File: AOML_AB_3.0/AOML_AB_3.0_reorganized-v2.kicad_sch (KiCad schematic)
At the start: 98 parts, among them IC11 SN74LVC1G3157DCKR, J1 Conn_01x04, J2 216550-1, J4 Conn_01x07, J5 Screw_Terminal_01x04, J6 Conn_01x03, J7 Screw_Terminal_01x07, SW1 TS02-66-70-BK-160-LCR-D, U1 L7812ABD2T-TR, U2 LM7805MPX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

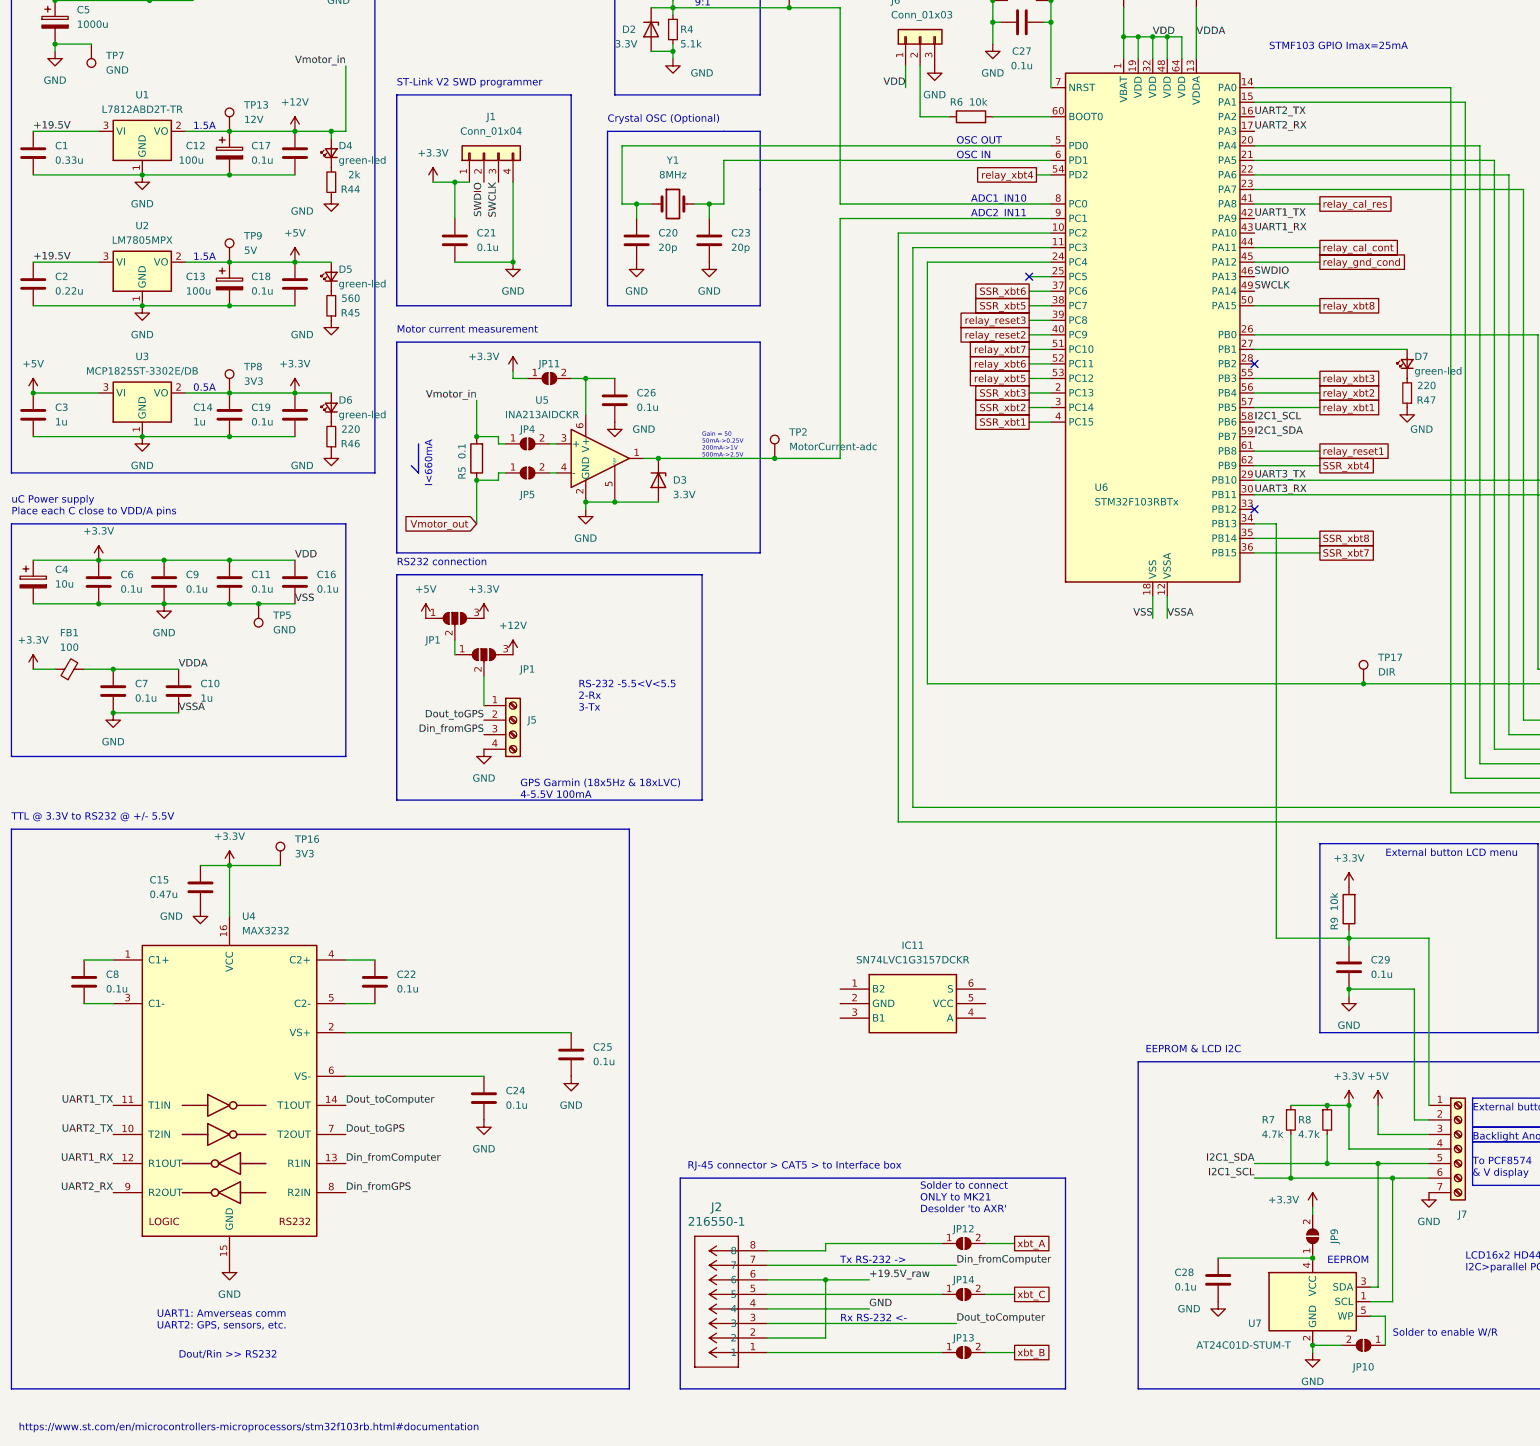
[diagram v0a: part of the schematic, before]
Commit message: PCB v2 final: added multiplexer for Tx (from STM32 uart1 OR GPS), GPS only 3 pins (pwr, gnd, Tx), Auxiliary test connectors RS232+PWR added, thin track thickness changed (0.15 to 0.155 mm)
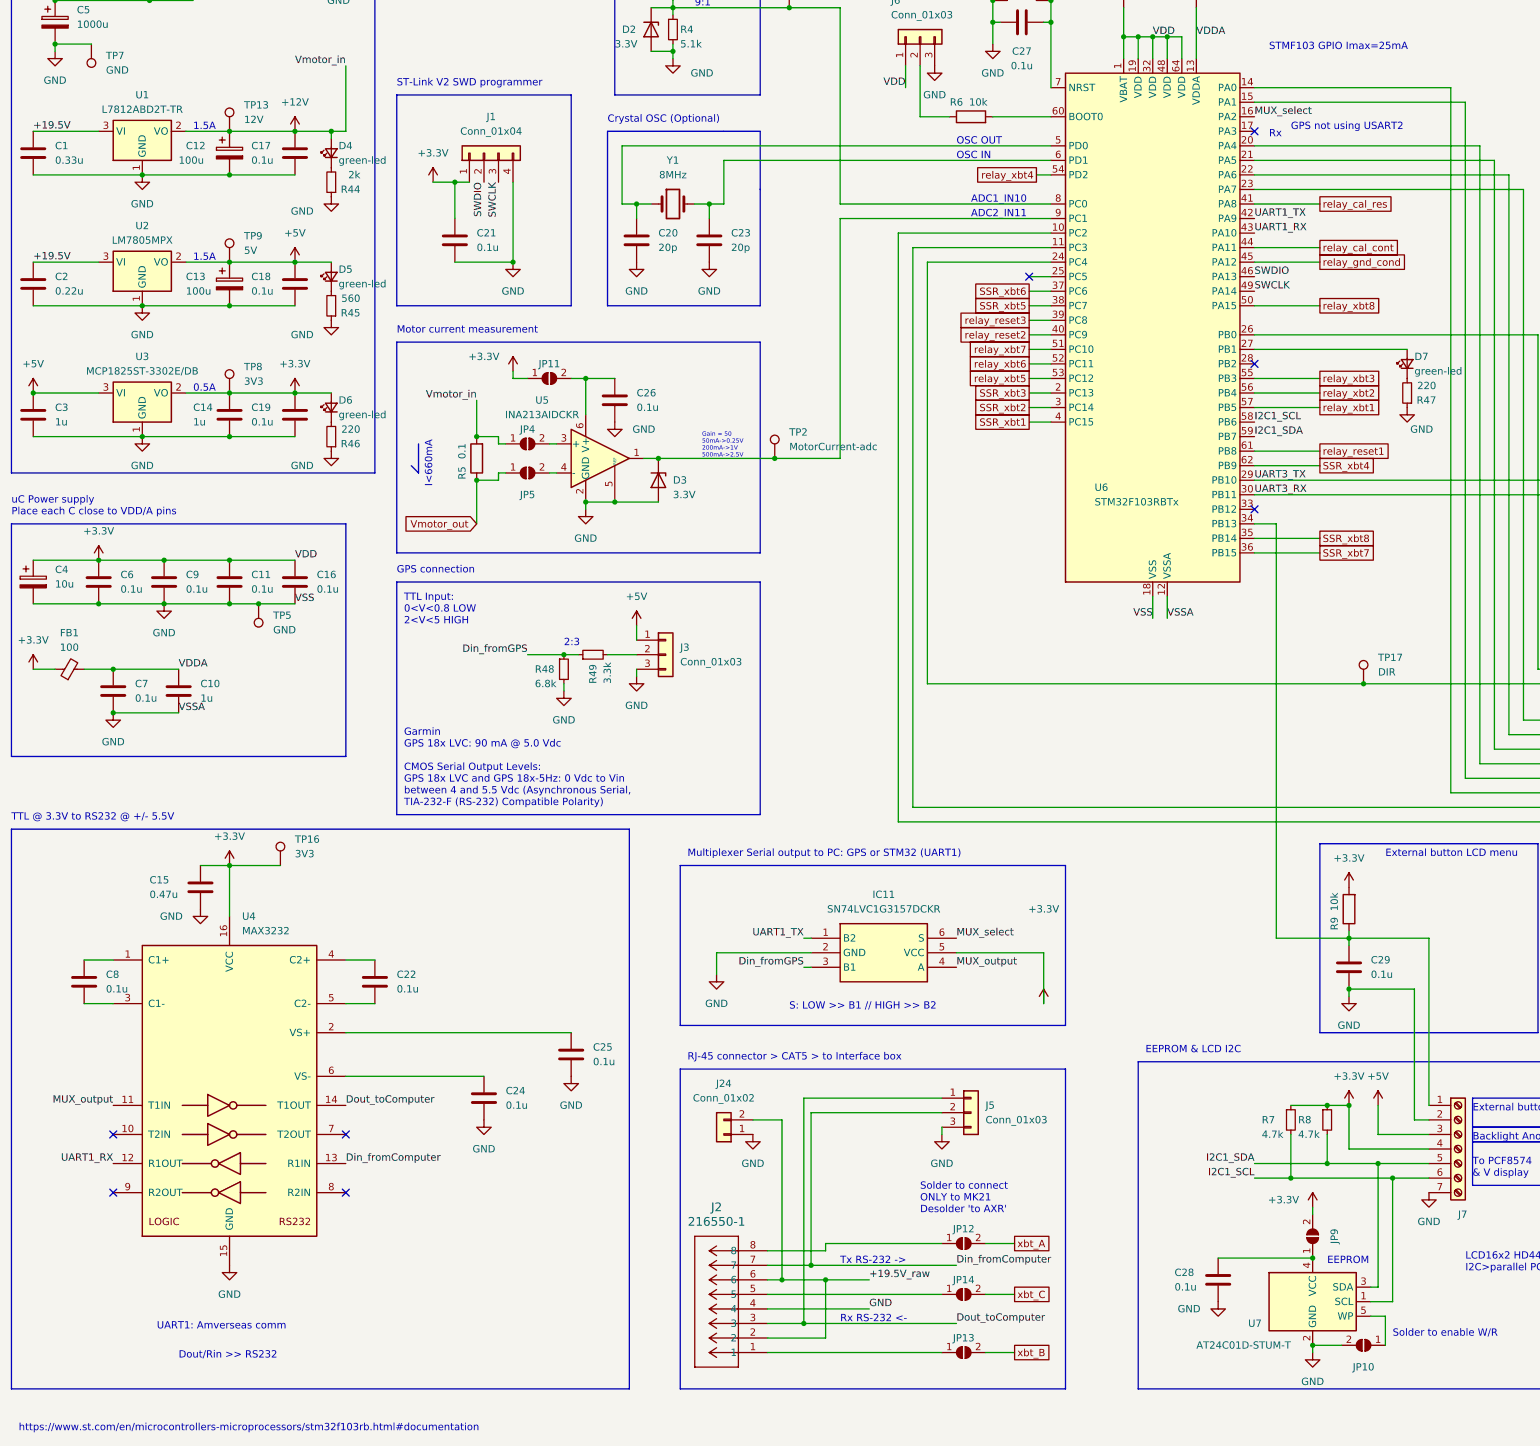
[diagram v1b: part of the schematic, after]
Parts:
- removed J5: Screw_Terminal_01x04, Header_screw_4x1_TB001-500-04BE:CUI_TB001-500-04BE, symbol Connector:Screw_Terminal_01x04
- removed JP1 (x2): SolderJumper_3_Open, Jumper:SolderJumper-3_P1.3mm_Open_RoundedPad1.0x1.5mm, symbol Jumper:SolderJumper_3_Open
- added J24: Conn_01x02, Connector_PinSocket_2.54mm:PinSocket_1x02_P2.54mm_Vertical, symbol Connector_Generic:Conn_01x02
- added J3: Conn_01x03, CUI_3x1_connector:CUI_TBP02R2-381-03BE, symbol Connector_Generic:Conn_01x03
- added J5: Conn_01x03, Connector_PinSocket_2.54mm:PinSocket_1x03_P2.54mm_Vertical, symbol Connector_Generic:Conn_01x03
- added R48: 6.8k, Resistor_0805:RC0805N_YAG, symbol Device:R_Small
- added R49: 3.3k, Resistor_0805:RC0805N_YAG, symbol Device:R_Small
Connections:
- net +19.5V_raw: now also J24.2 (Pin_2)
- net +3.3V: now also IC11.5 (VCC)
- net +5V: now also J3.1 (Pin_1)
- net Din_fromComputer: now also J5.2 (Pin_2)
- net Din_fromGPS: now also IC11.3 (B1), R48.1, R49.1; no longer U4.8 (R2IN)
- net Dout_toComputer: now also J5.1 (Pin_1)
- net GND: now also IC11.2 (GND), J24.1 (Pin_1), J3.3 (Pin_3), J5.3 (Pin_3), R48.2
- net UART1_TX: now also IC11.1 (B2); no longer U4.11 (T1IN)
- net MUX_output: now reaches IC11.4 (A)
- net MUX_output: now also U4.11 (T1IN)
- net MUX_select: now reaches IC11.6 (S)
- net MUX_select: now also U6.16 (PA2)
- net Dout_toGPS: no longer names the net of U4.7 (T2OUT)
- net UART2_RX: no longer names the net of U4.9 (R2OUT)
- net UART2_RX: no longer U6.17 (PA3)
- net UART2_TX: no longer names the net of U4.10 (T2IN)
- net UART2_TX: no longer U6.16 (PA2)
- new net: J3.2 (Pin_2), R49.2
- no-connect marks 3 -> 8
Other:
- note added: "GPS connection"
- note added: "GPS not using USART2"
- note added: "Garmin GPS 18x LVC: 90 mA @ 5.0 Vdc CMOS Serial Output Levels: GPS 18x LVC and GPS 18x-5Hz: 0 Vdc to Vin between 4 and 5.5 Vdc (Asynchronous Serial, TIA-232-F (RS-232) Compatible Polarity)"
- note added: "Multiplexer Serial output to PC: GPS or STM32 (UART1)"
- note added: "Rx"
- note added: "S: LOW >> B1 // HIGH >> B2"
- note added: "TTL Input: 0<V<0.8 LOW 2<V<5 HIGH"
- note added: "UART1: Amverseas comm"
- note removed: "GPS Garmin (18x5Hz & 18xLVC) 4-5.5V 100mA"
- note removed: "RS-232 -5.5<V<5.5 2-Rx 3-Tx"
- note removed: "RS232 connection"
- note removed: "UART1: Amverseas comm UART2: GPS, sensors, etc."
- moved on the sheet: IC11

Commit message: New version v3, in assembly process and noting changes for next revision
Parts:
- added FID1, FID2, FID3: Fiducial, Fiducial:Fiducial_0.75mm_Mask1.5mm, symbol Mechanical:Fiducial
- IC11: Cost (none) -> 0.34; Digikey (none) -> https://www.digikey.com/en/products/detail/texas-instrument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; Height 1.1 -> (none); Manufacturer_Name Texas Instruments -> (none); Manufacturer_Part_Number SN74LVC1G3157DCKR -> (none); Mouser Part Number 595-SN74LVC1G3157DCK -> (none); Mouser Price/Stock https://www.mouser.co.uk/ProductDetail/Texas-Instruments/SN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 -> (none)
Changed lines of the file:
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@@
     )
   )
+  (symbol (lib_id "Mechanical:Fiducial") (at 304.8 46.99 0) (unit 1)
+    (in_bom yes) (on_board yes) (dnp no) (fields_autoplaced)
+    (property "Reference" "FID3" (at 307.34 45.72 0)
+      (effects (font (size 1.27 1.27)) (justify left))
+    )
+    (property "Value" "Fiducial" (at 307.34 48.26 0)
+      (effects (font (size 1.27 1.27)) (justify left))
+    )
+    (property "Footprint" "Fiducial:Fiducial_0.75mm_Mask1.5mm" (at 304.8 46.99 0)
+      (effects (font (size 1.27 1.27)) hide)
+    )
+    (property "Datasheet" "~" (at 304.8 46.99 0)
+      (effects (font (size 1.27 1.27)) hide)
+    )
+    (instances
+      (project "AOML_AB_3.0_reorganized-v2"
+        (path "/6a222f58-627e-41ff-951d-9ad8d2e0d7a2"
+          (reference "FID3") (unit 1)
+        )
+      )
+    )
+  )
   (symbol (lib_id "power:GND") (at 175.26 44.45 0) (unit 1)
     (in_bom yes) (on_board yes) (dnp no) (fields_autoplaced)
@@
       (effects (font (size 1.27 1.27)) hide)
     )
-    (property "Datasheet" "" (at 69.85 109.22 0)
+    (property "Datasheet" "https://www.yageo.com/upload/media/product/products/datasheet/rchip/PYu-RC_Group_51_RoHS_L_12.pdf" (at 69.85 109.22 0)
       (effects (font (size 1.27 1.27)) hide)
     )
@@
       (effects (font (size 1.27 1.27)) hide)
     )
-    (property "Datasheet" "" (at 257.81 101.6 0)
+    (property "Datasheet" "https://www.yageo.com/upload/media/product/products/datasheet/rchip/PYu-RC_Group_51_RoHS_L_12.pdf" (at 257.81 101.6 0)
       (effects (font (size 1.27 1.27)) hide)
     )
@@
     )
   )
+  (symbol (lib_id "Mechanical:Fiducial") (at 304.8 31.75 0) (unit 1)
+    (in_bom yes) (on_board yes) (dnp no) (fields_autoplaced)
+    (property "Reference" "FID1" (at 307.34 30.48 0)
+      (effects (font (size 1.27 1.27)) (justify left))
+    )
+    (property "Value" "Fiducial" (at 307.34 33.02 0)
+      (effects (font (size 1.27 1.27)) (justify left))
+    )
+    (property "Footprint" "Fiducial:Fiducial_0.75mm_Mask1.5mm" (at 304.8 31.75 0)
+      (effects (font (size 1.27 1.27)) hide)
+    )
+    (property "Datasheet" "~" (at 304.8 31.75 0)
+      (effects (font (size 1.27 1.27)) hide)
+    )
+    (instances
+      (project "AOML_AB_3.0_reorganized-v2"
+        (path "/6a222f58-627e-41ff-951d-9ad8d2e0d7a2"
+          (reference "FID1") (unit 1)
+        )
+      )
+    )
+  )
   (symbol (lib_id "Connector:TestPoint") (at 57.15 138.43 180) (unit 1)
     (in_bom yes) (on_board yes) (dnp no) (fields_autoplaced)
@@
       (effects (font (size 1.27 1.27)) (justify left top) hide)
     )
-    (property "Height" "1.1" (at 175.26 591.77 0)
-      (effects (font (size 1.27 1.27)) (justify left top) hide)
-    )
-    (property "Mouser Part Number" "595-SN74LVC1G3157DCK" (at 175.26 691.77 0)
-      (effects (font (size 1.27 1.27)) (justify left top) hide)
-    )
-    (property "Mouser Price/Stock" "https://www.mouser.co.uk/ProductDetail/Texas-Instruments/SN74LVC1G3157DCKR?qs=PVVDbbWpW3J21wbz0QWbxg%3D%3D" (at 175.26 791.77 0)
-      (effects (font (size 1.27 1.27)) (justify left top) hide)
-    )
-    (property "Manufacturer_Name" "Texas Instruments" (at 175.26 891.77 0)
-      (effects (font (size 1.27 1.27)) (justify left top) hide)
+    (property "Cost" "0.34" (at 153.67 196.85 0)
+      (effects (font (size 1.27 1.27)) hide)
     )
-    (property "Manufacturer_Part_Number" "SN74LVC1G3157DCKR" (at 175.26 991.77 0)
-      (effects (font (size 1.27 1.27)) (justify left top) hide)
+    (property "Digikey" "https://www.digikey.com/en/products/detail/texas-instruments/SN74LVC1G3157DCKR/562895" (at 153.67 196.85 0)
+      (effects (font (size 1.27 1.27)) hide)
     )
     (pin "1")
@@
       (effects (font (size 1.27 1.27)) hide)
     )
-    (property "Datasheet" "" (at 69.85 64.77 0)
+    (property "Datasheet" "https://www.yageo.com/upload/media/product/products/datasheet/rchip/PYu-RC_Group_51_RoHS_L_12.pdf" (at 69.85 64.77 0)
       (effects (font (size 1.27 1.27)) hide)
     )
@@
       (effects (font (size 1.27 1.27)) hide)
     )
-    (property "Datasheet" "" (at 69.85 86.36 0)
+    (property "Datasheet" "https://www.yageo.com/upload/media/product/products/datasheet/rchip/PYu-RC_Group_51_RoHS_L_12.pdf" (at 69.85 86.36 0)
       (effects (font (size 1.27 1.27)) hide)
     )
@@
       (effects (font (size 1.27 1.27)) hide)
     )
-    (property "Datasheet" "~" (at 17.78 82.55 0)
+    (property "Datasheet" "https://mm.digikey.com/Volume0/opasdata/d220001/medias/docus/6128/CL21B224KBFNNNE.pdf" (at 17.78 82.55 0)
       (effects (font (size 1.27 1.27)) hide)
     )
@@
         )
       )
+    )
+  )
+  (symbol (lib_id "Mechanical:Fiducial") (at 304.8 39.37 0) (unit 1)
+    (in_bom yes) (on_board yes) (dnp no) (fields_autoplaced)
+    (property "Reference" "FID2" (at 307.34 38.1 0)
+      (effects (font (size 1.27 1.27)) (justify left))
+    )
+    (property "Value" "Fiducial" (at 307.34 40.64 0)
+      (effects (font (size 1.27 1.27)) (justify left))
+    )
+    (property "Footprint" "Fiducial:Fiducial_0.75mm_Mask1.5mm" (at 304.8 39.37 0)
+      (effects (font (size 1.27 1.27)) hide)
+    )
+    (property "Datasheet" "~" (at 304.8 39.37 0)
+      (effects (font (size 1.27 1.27)) hide)
+    )
+    (instances
+      (project "AOML_AB_3.0_reorganized-v2"
+        (path "/6a222f58-627e-41ff-951d-9ad8d2e0d7a2"
+          (reference "FID2") (unit 1)
+        )
+      )
